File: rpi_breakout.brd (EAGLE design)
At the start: 34.4 x 38.4 mm, 20 parts

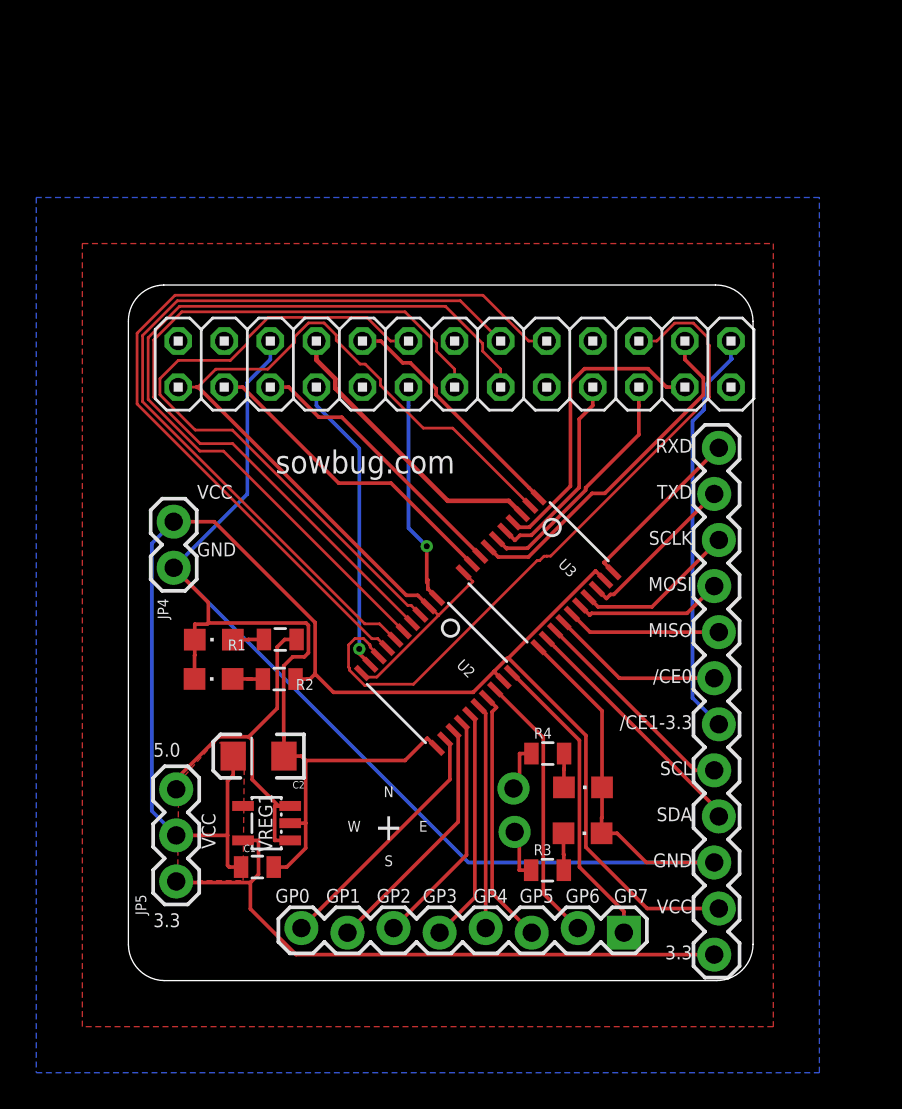
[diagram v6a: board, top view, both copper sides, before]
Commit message: Moved 26 pin header NW.  7 vias.
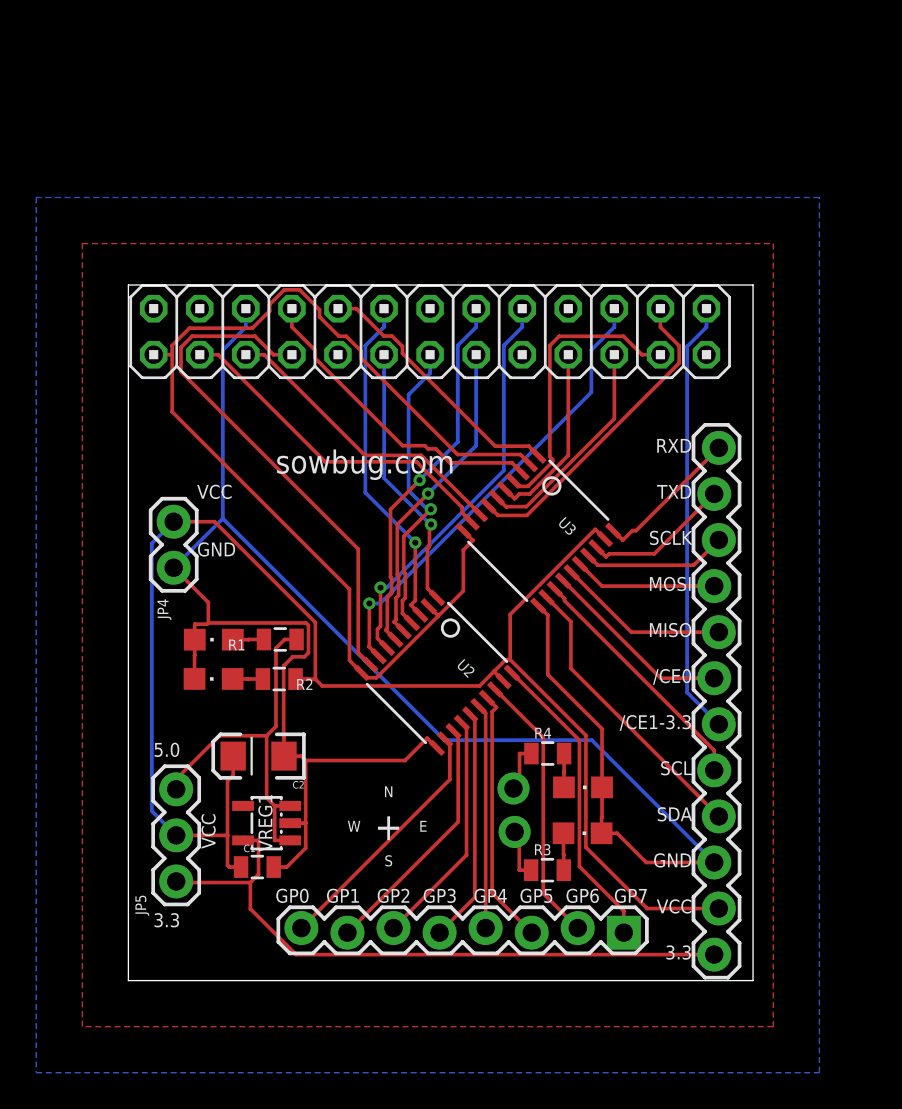
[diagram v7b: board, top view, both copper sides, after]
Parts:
- moved U3 2.29 mm to (22.6, 24.8)
- moved JP1 2.24 mm to (16.6, 35.8)
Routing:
- net GPIO_3: track 45.6 -> 17.4 mm, vias 0 -> 1
- net GPIO_2: track 42.3 -> 16.8 mm, vias 0 -> 1
- net GPIO_5: track 47.8 -> 22.4 mm, vias 0 -> 1
- net GPIO_4: track 44.5 -> 20.6 mm, vias 0 -> 1
- net GPIO_1: track 36.1 -> 18.8 mm, vias 0 -> 1
- net GPIO_6: track 38.4 -> 25.3 mm, vias 0 -> 1
- net GPIO_7: track 16.5 -> 28.6 mm, vias 1 -> 0
- net 3V3_RPI: track 53.2 -> 61.2 mm
- net GPIO_0: track 12.5 -> 14.8 mm
- net SDAV0: track 13.7 -> 16.0 mm
- net VCC: track 83.3 -> 85.4 mm
- net GND: track 108.4 -> 110.3 mm
- net SCLV0: track 12.0 -> 13.6 mm
- net RXDV: track 9.71 -> 8.15 mm
- net /SPI_CE0: track 19.1 -> 17.7 mm
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- removed copper zone on layer 1, net VCC
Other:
- outline, holes or cut-outs redrawn

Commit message: Split special-pin header into 2x6.
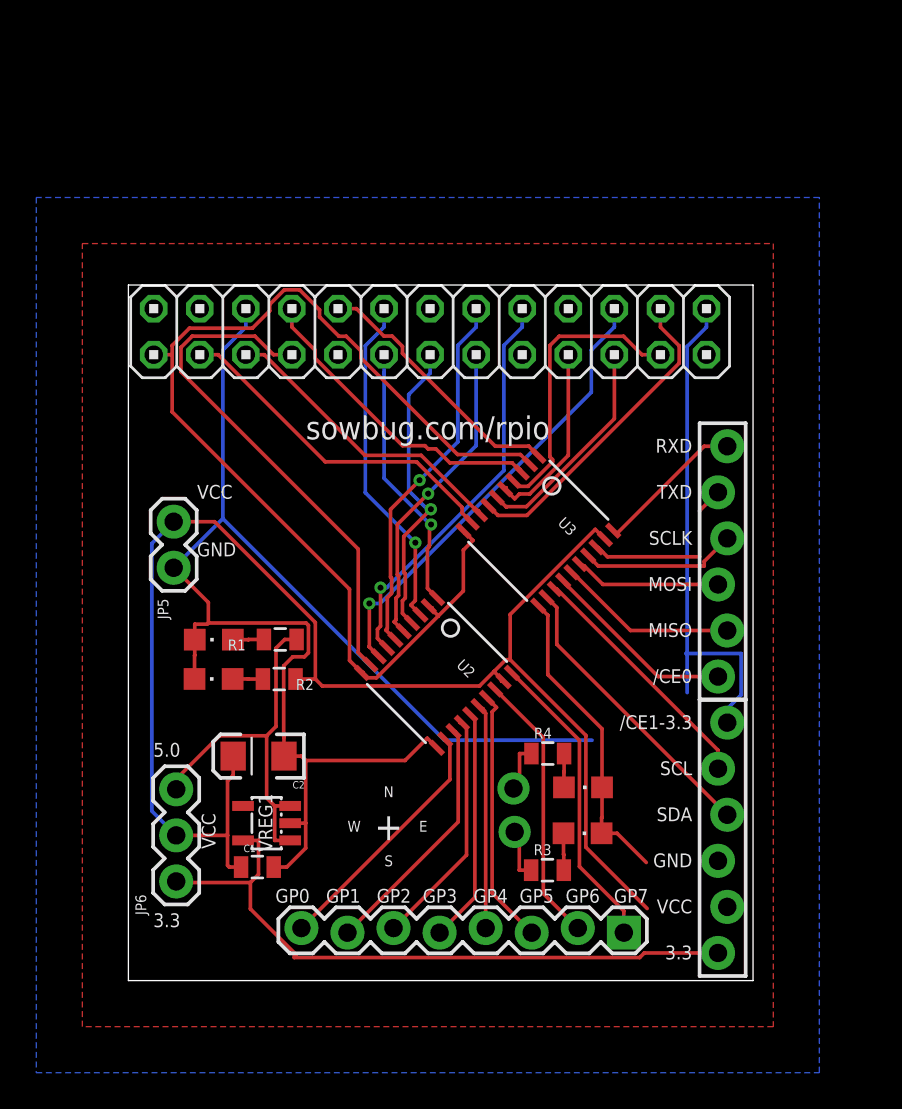
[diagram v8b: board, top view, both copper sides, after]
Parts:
- added JP8: (no value), adafruit:1X01-CLEANBIG
- JP3: value COMM -> (none); device SparkFun:1X12_LOCK -> SparkFun:1X06_FEMALE_LOCK.010
- JP4: value IO-PWR-EXT -> (none); device SparkFun:1X02 -> SparkFun:1X06_FEMALE_LOCK.010
- JP5: value VTG-SEL -> IO-PWR-EXT; device SparkFun:1X03 -> SparkFun:1X02
- JP6: value (none) -> VTG-SEL; device adafruit:1X01-CLEANBIG -> SparkFun:1X03
- moved JP4 31.5 mm to (32.8, 16.8), turned to 90 degrees
- moved JP5 19.8 mm to (2.50, 25.3), turned to 270 degrees
- moved JP6 18.9 mm to (2.64, 5.47), turned to 90 degrees
- moved JP7 2.40 mm to (21.3, 8.20)
- moved JP3 0.35 mm to (32.8, 1.52)
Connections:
- net N$3 renamed LED3_A
- net N$5 renamed LED4_A
- removed net N$4: JP6.1, R3.1
- removed net N$6: JP7.1, R4.1
- new net LED3_JP: JP7.1, R3.1
- new net LED4_JP: JP8.1, R4.1
- net /SPI_CEV0: now also JP4.1; no longer JP3.7
- net 3.3V: now also JP6.1; no longer JP5.1
- net 5V: now also JP6.3; no longer JP5.3
- net GND: now also JP5.2; no longer JP4.2
- net RXDV: now also JP4.6; no longer JP3.12
- net SPI_MISOV: now also JP4.2; no longer JP3.8
- net SPI_MOSIV: now also JP4.3; no longer JP3.9
- net SPI_SCLKV: now also JP4.4; no longer JP3.10
- net TXDV: now also JP4.5; no longer JP3.11
- net VCC: now also JP5.1, JP6.2; no longer JP4.1, JP5.2
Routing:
- net GND: track 110.3 -> 97.0 mm
- net /SPI_CE1: track 24.1 -> 28.8 mm
- net VCC: track 85.4 -> 81.6 mm
- net N$4: track 2.87 -> 0.00 mm
- net LED3_JP: track 0.00 -> 2.87 mm
- net N$6: track 2.72 -> 0.00 mm
- net LED4_JP: track 0.00 -> 2.72 mm
- net TXDV: track 8.15 -> 9.87 mm
- net 3V3_RPI: track 61.2 -> 62.1 mm
- net SPI_SCLKV: track 8.00 -> 8.69 mm
- net 3.3V: track 35.6 -> 36.2 mm
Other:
- board text added: "RPio: Raspberry Pi Breakout Board"
- board text added: "sowbug.com/rpio"
- board text added: "v0.0.2"
- board text removed: "Raspberry Pi Breakout Board v0.0.2"
